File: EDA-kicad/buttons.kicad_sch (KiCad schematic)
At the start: 4 parts, among them SW2 PROG, SW3 VOL-, SW4 VOL+, SW5 POW

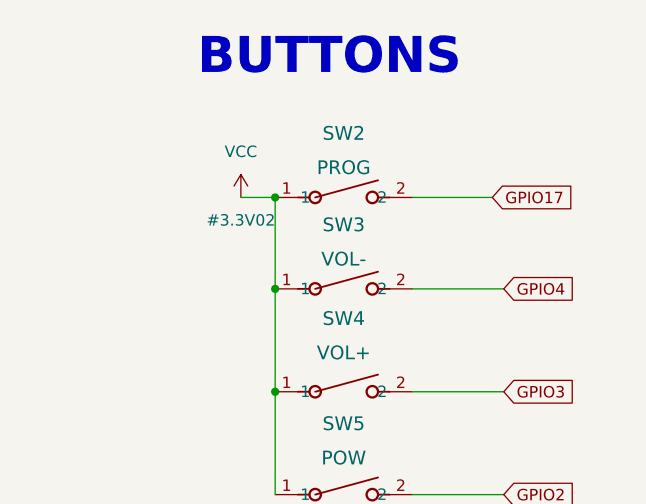
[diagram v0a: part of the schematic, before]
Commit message: reannotate entire schematic
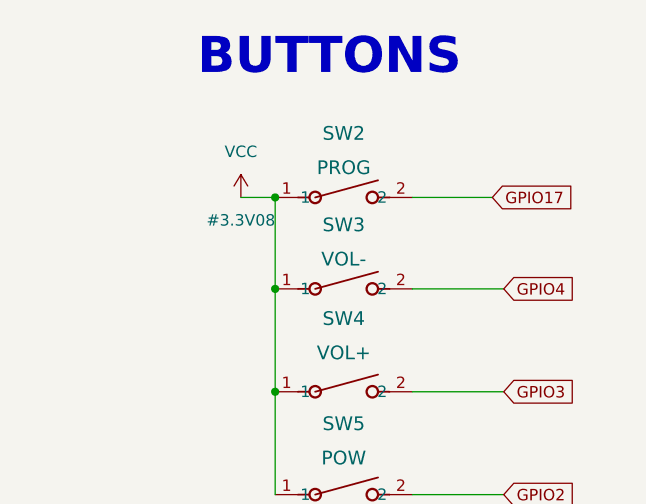
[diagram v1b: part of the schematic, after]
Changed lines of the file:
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@@
 		(on_board yes)
 		(dnp no)
-		(property "Reference" "#3.3V02"
+		(property "Reference" "#3.3V08"
 			(at 119.38 77.47 0)
 			(effects
@@
 			(project "cm5-carrier"
 				(path "/28c5e4fe-1ec7-4477-97f0-d2ec1401fad5/7d72c53e-b066-4e49-bdb9-37372138f009"
-					(reference "#3.3V02")
+					(reference "#3.3V08")
 					(unit 1)
 				)

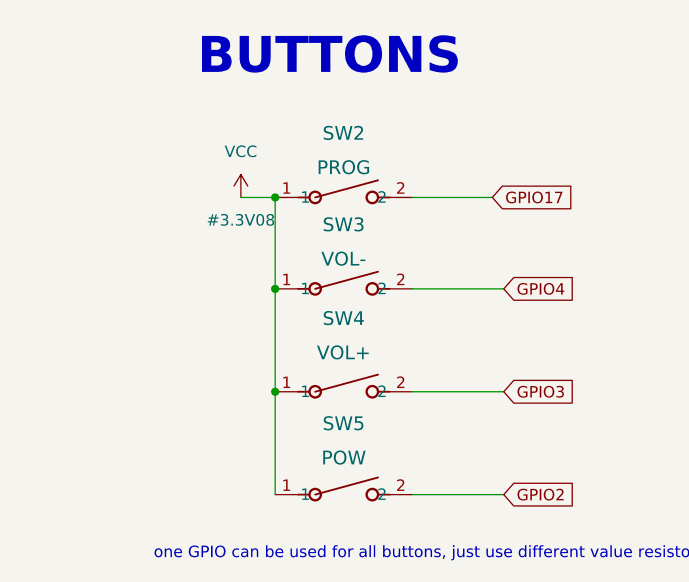
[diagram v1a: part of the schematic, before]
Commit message: add new switches and reannotate
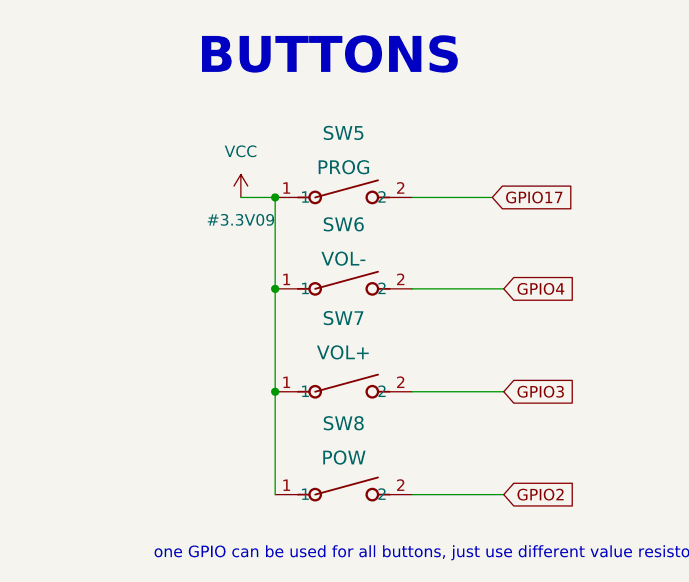
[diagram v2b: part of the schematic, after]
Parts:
- renumbered SW2 to SW5, SW3 to SW6, SW4 to SW7, SW5 to SW8
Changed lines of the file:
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@@
 		(dnp no)
 		(fields_autoplaced yes)
-		(property "Reference" "SW2"
+		(property "Reference" "SW5"
 			(at 130.81 67.818 0)
 			(effects
@@
 			(project "cm5-carrier"
 				(path "/28c5e4fe-1ec7-4477-97f0-d2ec1401fad5/7d72c53e-b066-4e49-bdb9-37372138f009"
-					(reference "SW2")
+					(reference "SW5")
 					(unit 1)
 				)
@@
 		(on_board yes)
 		(dnp no)
-		(property "Reference" "#3.3V08"
+		(property "Reference" "#3.3V09"
 			(at 119.38 77.47 0)
 			(effects
@@
 			(project "cm5-carrier"
 				(path "/28c5e4fe-1ec7-4477-97f0-d2ec1401fad5/7d72c53e-b066-4e49-bdb9-37372138f009"
-					(reference "#3.3V08")
+					(reference "#3.3V09")
 					(unit 1)
 				)
@@
 		(dnp no)
 		(fields_autoplaced yes)
-		(property "Reference" "SW4"
+		(property "Reference" "SW7"
 			(at 130.81 88.392 0)
 			(effects
@@
 			(project "cm5-carrier"
 				(path "/28c5e4fe-1ec7-4477-97f0-d2ec1401fad5/7d72c53e-b066-4e49-bdb9-37372138f009"
-					(reference "SW4")
+					(reference "SW7")
 					(unit 1)
 				)
@@
 		(dnp no)
 		(fields_autoplaced yes)
-		(property "Reference" "SW3"
+		(property "Reference" "SW6"
 			(at 130.81 77.978 0)
 			(effects
@@
 			(project "cm5-carrier"
 				(path "/28c5e4fe-1ec7-4477-97f0-d2ec1401fad5/7d72c53e-b066-4e49-bdb9-37372138f009"
-					(reference "SW3")
+					(reference "SW6")
 					(unit 1)
 				)
@@
 		(dnp no)
 		(fields_autoplaced yes)
-		(property "Reference" "SW5"
+		(property "Reference" "SW8"
 			(at 130.81 100.076 0)
 			(effects
@@
 			(project "cm5-carrier"
 				(path "/28c5e4fe-1ec7-4477-97f0-d2ec1401fad5/7d72c53e-b066-4e49-bdb9-37372138f009"
-					(reference "SW5")
-					(unit 1)
-				)
+					(reference "SW8")
+					(unit 1)
+				)

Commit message: POWER SCHEMATIC FINISHED
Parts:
- renumbered SW5 to SW4, SW6 to SW5, SW7 to SW6, SW8 to SW7
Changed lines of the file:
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@@
 		(dnp no)
 		(fields_autoplaced yes)
-		(property "Reference" "SW5"
+		(property "Reference" "SW4"
 			(at 130.81 67.818 0)
 			(effects
@@
 			(project "cm5-carrier"
 				(path "/28c5e4fe-1ec7-4477-97f0-d2ec1401fad5/7d72c53e-b066-4e49-bdb9-37372138f009"
-					(reference "SW5")
+					(reference "SW4")
 					(unit 1)
 				)
@@
 		(dnp no)
 		(fields_autoplaced yes)
-		(property "Reference" "SW7"
+		(property "Reference" "SW6"
 			(at 130.81 88.392 0)
 			(effects
@@
 			(project "cm5-carrier"
 				(path "/28c5e4fe-1ec7-4477-97f0-d2ec1401fad5/7d72c53e-b066-4e49-bdb9-37372138f009"
-					(reference "SW7")
+					(reference "SW6")
 					(unit 1)
 				)
@@
 		(dnp no)
 		(fields_autoplaced yes)
-		(property "Reference" "SW6"
+		(property "Reference" "SW5"
 			(at 130.81 77.978 0)
 			(effects
@@
 			(project "cm5-carrier"
 				(path "/28c5e4fe-1ec7-4477-97f0-d2ec1401fad5/7d72c53e-b066-4e49-bdb9-37372138f009"
-					(reference "SW6")
+					(reference "SW5")
 					(unit 1)
 				)
@@
 		(dnp no)
 		(fields_autoplaced yes)
-		(property "Reference" "SW8"
+		(property "Reference" "SW7"
 			(at 130.81 100.076 0)
 			(effects
@@
 			(project "cm5-carrier"
 				(path "/28c5e4fe-1ec7-4477-97f0-d2ec1401fad5/7d72c53e-b066-4e49-bdb9-37372138f009"
-					(reference "SW8")
-					(unit 1)
-				)
+					(reference "SW7")
+					(unit 1)
+				)

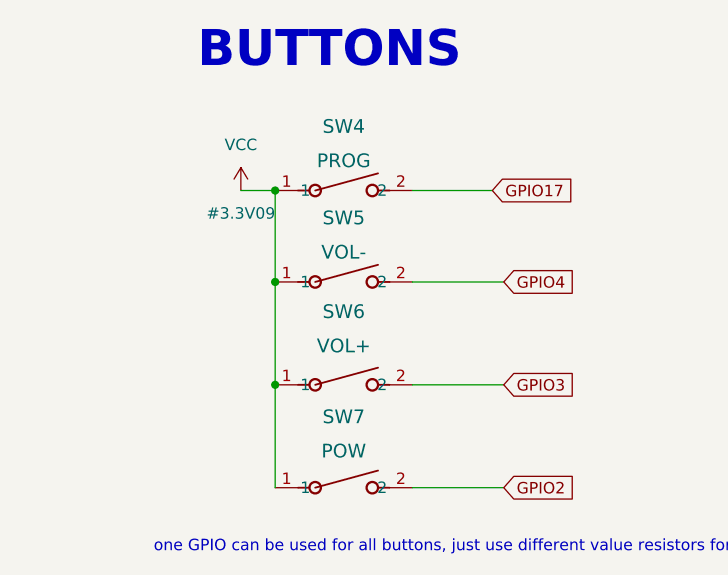
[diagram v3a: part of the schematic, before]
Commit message: set everything except from power to DNP
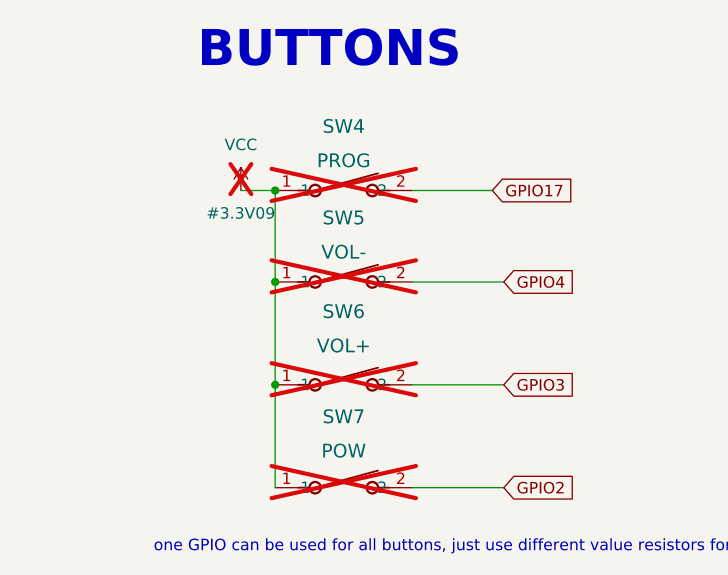
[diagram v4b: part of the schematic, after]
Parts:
- SW4, SW5, SW6, SW7: now not fitted

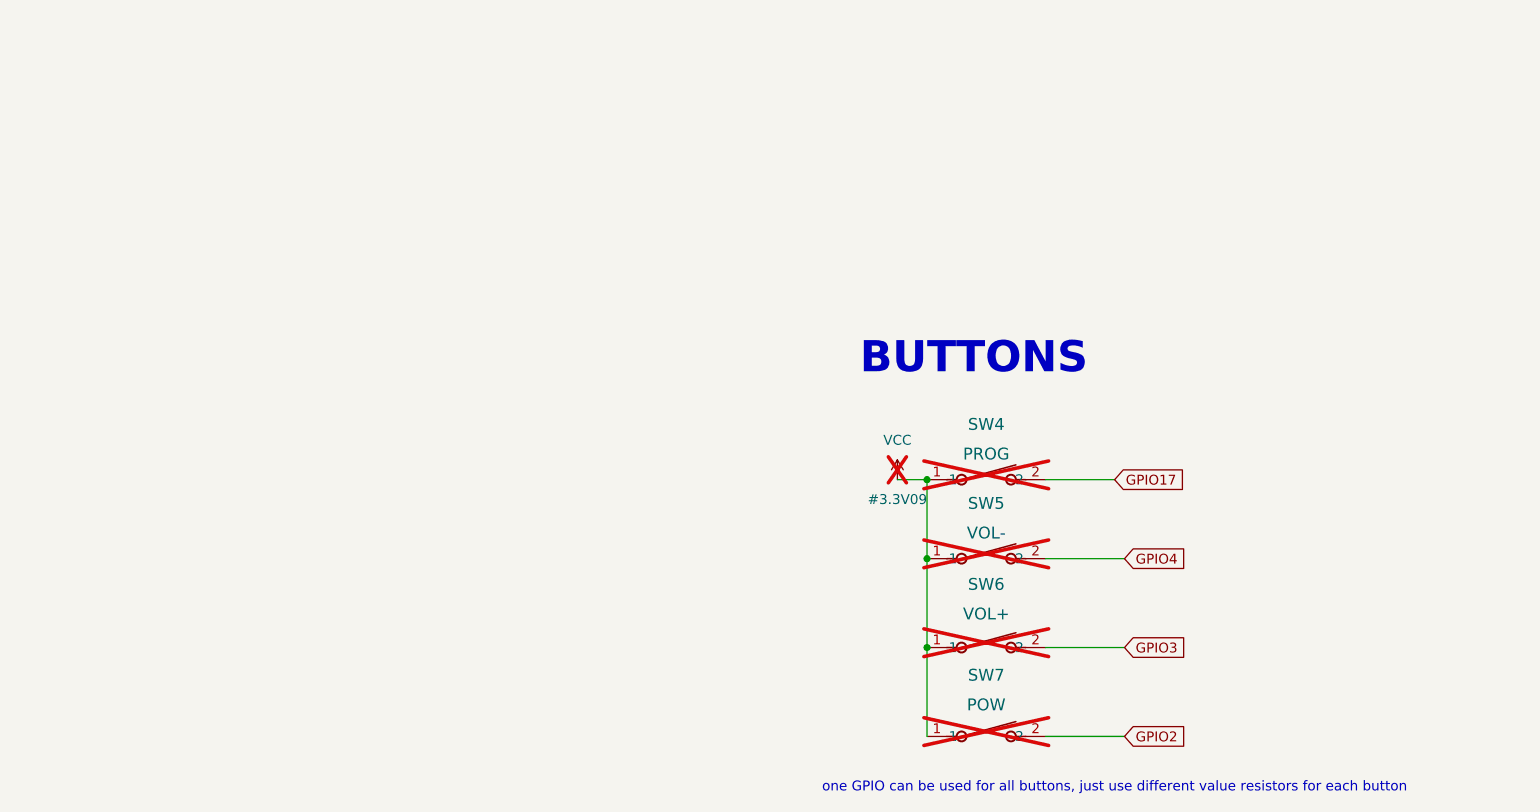
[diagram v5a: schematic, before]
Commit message: Reduced the GPIO usage for the Buttons and redone the LED
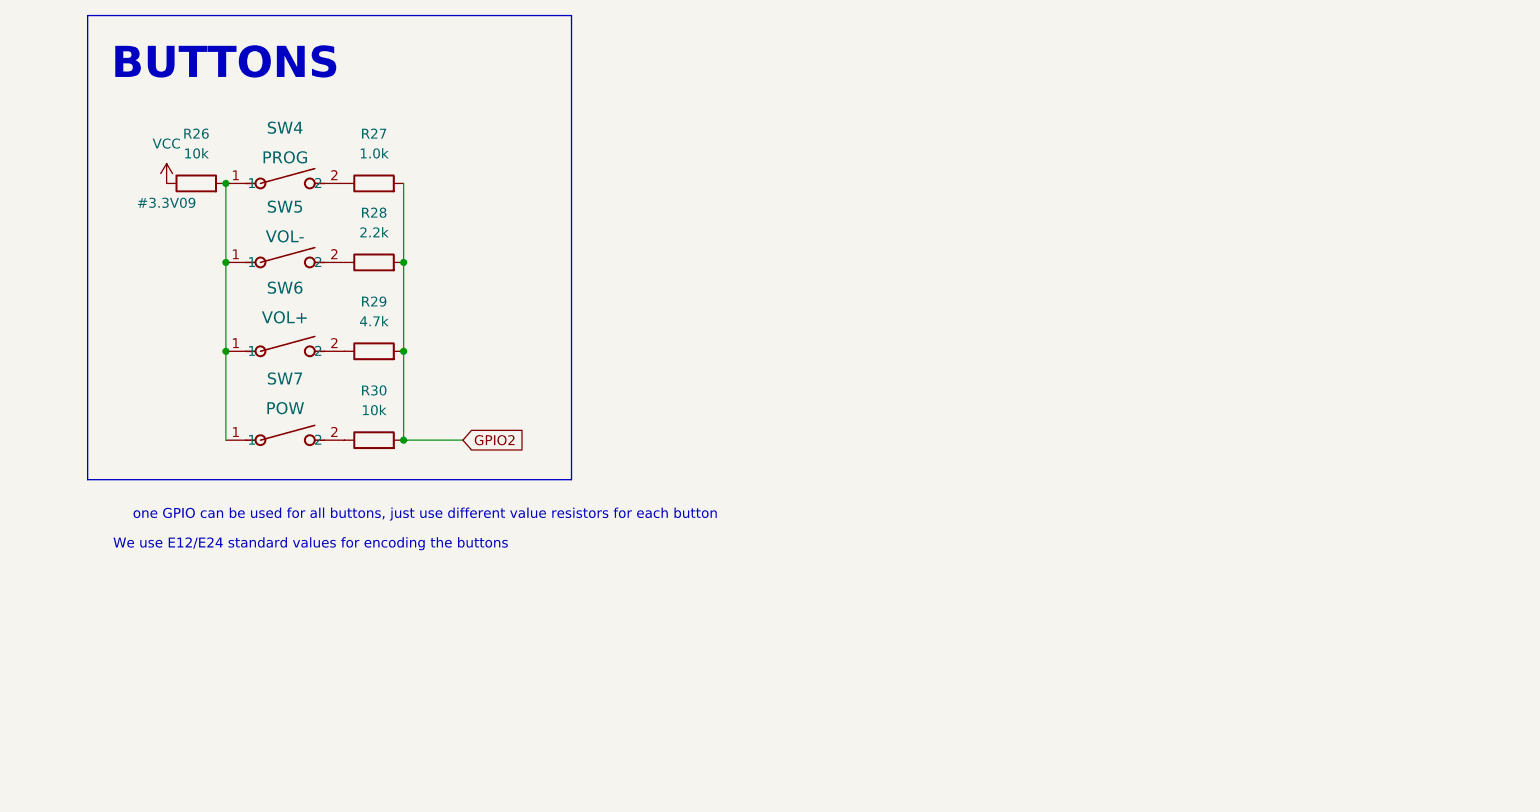
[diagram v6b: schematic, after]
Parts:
- added R26, R30: 10k, symbol Device:R
- added R27: 1.0k, symbol Device:R
- added R28: 2.2k, symbol Device:R
- added R29: 4.7k, symbol Device:R
- SW4, SW5, SW6, SW7: now fitted
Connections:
- net GPIO2: now also R27.2, R28.2, R29.2, R30.2; no longer SW7.2
- net VCC: now also R26.1; no longer SW4.1, SW5.1, SW6.1, SW7.1
- net GPIO17: no longer names the net of SW4.2
- net GPIO17: now also R27.1
- net GPIO3: no longer names the net of SW6.2
- net GPIO3: now also R29.1
- net GPIO4: no longer names the net of SW5.2
- net GPIO4: now also R28.1
- new net: R26.2, SW4.1, SW5.1, SW6.1, SW7.1
- new net: R30.1, SW7.2
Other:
- note added: "We use E12/E24 standard values for encoding the buttons"
